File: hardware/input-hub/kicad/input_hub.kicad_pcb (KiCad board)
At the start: 2 copper layers, 116 x 49.1 mm, 38 parts, among them J1 ACJMIH, J2 ACJMIH, J3 ACJMIH, J5 8P8C, J6 BM04B-SRSS-TB_LF__SN_, J7 Conn_01x04, J8 Conn_01x02, P1 S2B-PH-SM4-TB_LF__SN_, U1 102010448, U2 TPD4E05U06DQAR, U3 TPD4E05U06DQAR

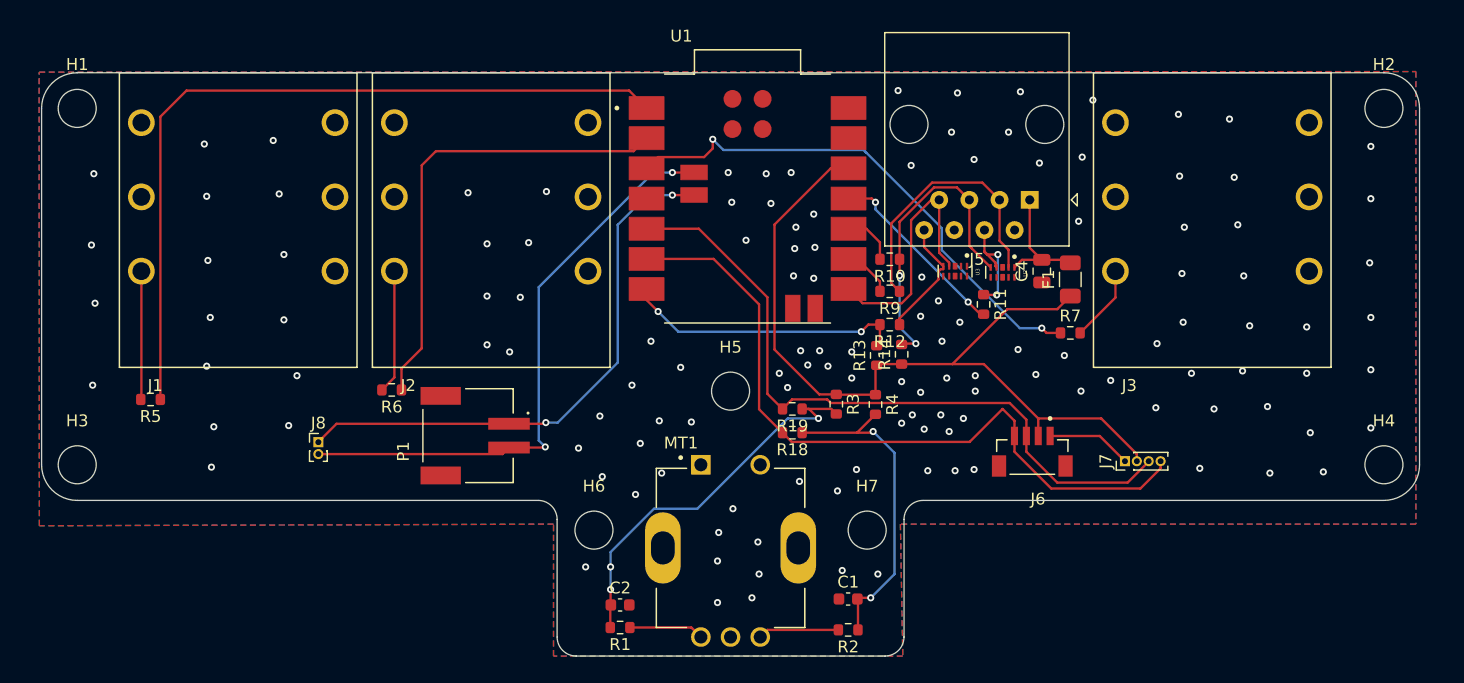
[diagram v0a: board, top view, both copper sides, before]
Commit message: fix: refine input hub board draft
Update the input hub KiCad design after
  layout review.

  - Replace solder fallback headers with standard 2.54 mm footprints.
  - Clean up PMW3610 RJ45 routing, ESD placement, and local power conditioning.
  - Add optional SJ1-3523N 3.5 mm jack library assets for future pedal jack variants.
  - Preserve AS5600, EC11, footswitch, battery, and PMW3610 interface options for review.
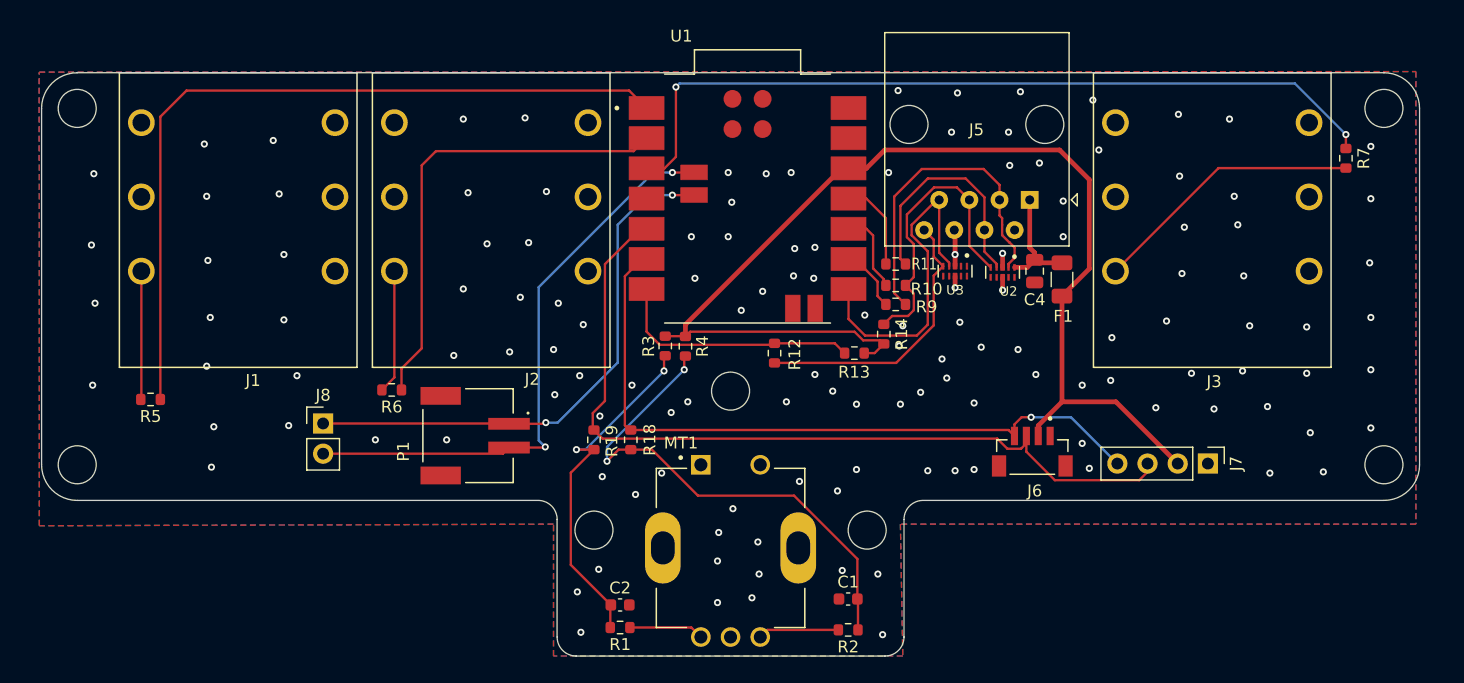
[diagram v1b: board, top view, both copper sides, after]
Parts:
- J7: footprint Connector_PinHeader_1.00mm:PinHeader_1x04_P1.00mm_Vertical -> Connector_PinHeader_2.54mm:PinHeader_1x04_P2.54mm_Vertical
- J8: footprint Connector_PinHeader_1.00mm:PinHeader_1x02_P1.00mm_Vertical -> Connector_PinHeader_2.54mm:PinHeader_1x02_P2.54mm_Vertical
- moved R7 27.5 mm to (206.8, 64.2), turned to -90 degrees
- moved R19 16.9 mm to (143.5, 87.9), turned to 90 degrees
- moved R4 16.7 mm to (151.2, 80.0)
- moved R3 15.2 mm to (149.5, 80.0)
- moved R18 13.6 mm to (146.6, 87.9), turned to 90 degrees
- moved R12 9.99 mm to (158.7, 80.6), turned to 90 degrees
- moved R11 8.14 mm to (168.9, 73.1), turned to 180 degrees
- moved J7 6.98 mm to (195.2, 89.9), turned to -90 degrees
- moved R14 2.27 mm to (167.9, 79.0)
- moved R10 2.26 mm to (168.9, 74.9)
- moved R13 1.89 mm to (165.4, 80.6), turned to 180 degrees
- moved J8 1.62 mm to (120.7, 86.5)
- moved R9 1.21 mm to (168.9, 76.5)
- moved F1 0.70 mm to (182.9, 74.4)
- moved C4 0.60 mm to (180.6, 73.7)
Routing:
- net +3V3: track 70.8 -> 98.3 mm
- net Button3: track 44.2 -> 68.2 mm
- net Net-(J3-PadT): track 6.43 -> 23.0 mm
- net Net-(C1-Pad2): track 27.6 -> 42.9 mm
- net NRST_RJ45: track 10.3 -> 23.7 mm
- net ENC_A: track 58.9 -> 70.5 mm
- net SDIO_RJ45: track 9.35 -> 20.1 mm, vias 2 -> 0
- net Net-(U1-D10/MOSI): track 15.8 -> 7.69 mm, vias 2 -> 0
- net MOT_RJ45: track 21.3 -> 28.2 mm
- net SCK_RJ45: track 23.1 -> 27.5 mm
- net Net-(C2-Pad1): track 33.3 -> 30.1 mm, vias 3 -> 2
- net Net-(U1-D6/TX): track 23.8 -> 21.1 mm, vias 2 -> 0
- net Net-(U1-D9/MISO): track 4.54 -> 6.88 mm
- net ENC_B: track 61.6 -> 59.8 mm, vias 0 -> 1
- net NCS_RJ45: track 26.3 -> 25.0 mm, vias 2 -> 0
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
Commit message: fix: refine input hub battery layout
- Update the battery connector layout.
  - Rename the battery connector from P to J.
  - Add return vias near signal vias.
  - Widen power-path traces.
  - Add XIAO battery solder holes and silkscreen labels.
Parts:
- added J10: Conn_01x01_Pin, Connector_Pin:Pin_D0.7mm_L6.5mm_W1.8mm_FlatFork, F.Cu at (151.9, 67.3)
- added J9: Conn_01x01_Pin, Connector_Pin:Pin_D0.7mm_L6.5mm_W1.8mm_FlatFork, F.Cu at (151.9, 65.4)
- moved J8 16.3 mm to (137.0, 86.3)
- moved J11 7.23 mm to (129.1, 87.5)
- moved R6 6.11 mm to (132.6, 83.1)
- renumbered P1 to J11
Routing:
- net BAT+: track 46.1 -> 36.4 mm, vias 2 -> 0
- net Button2: track 39.5 -> 30.2 mm
- net BAT-: track 49.8 -> 45.8 mm, vias 2 -> 0
- net Net-(J2-PadT): track 10.4 -> 11.5 mm
- net ENC_A: track 70.5 -> 69.7 mm
- net GND: vias 136 -> 143
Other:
- board text added: "BAT+"
- board text added: "BAT-"

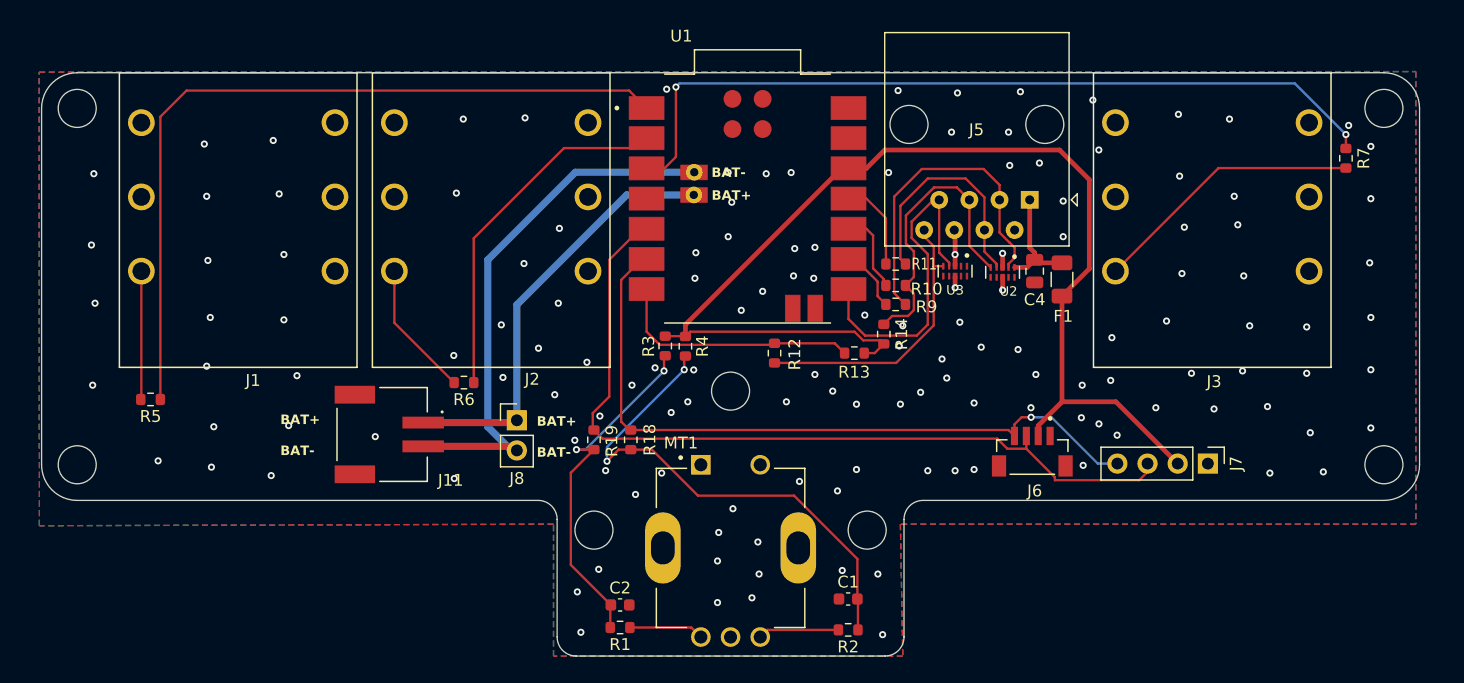
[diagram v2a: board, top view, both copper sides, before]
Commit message: fix: make input hub routing more gooder and a schematic change - esd routing and schematic - PEC11R debounce circuit - reduced back side routing - added filter caps to 1/4 inch jacks - made traces thiccer
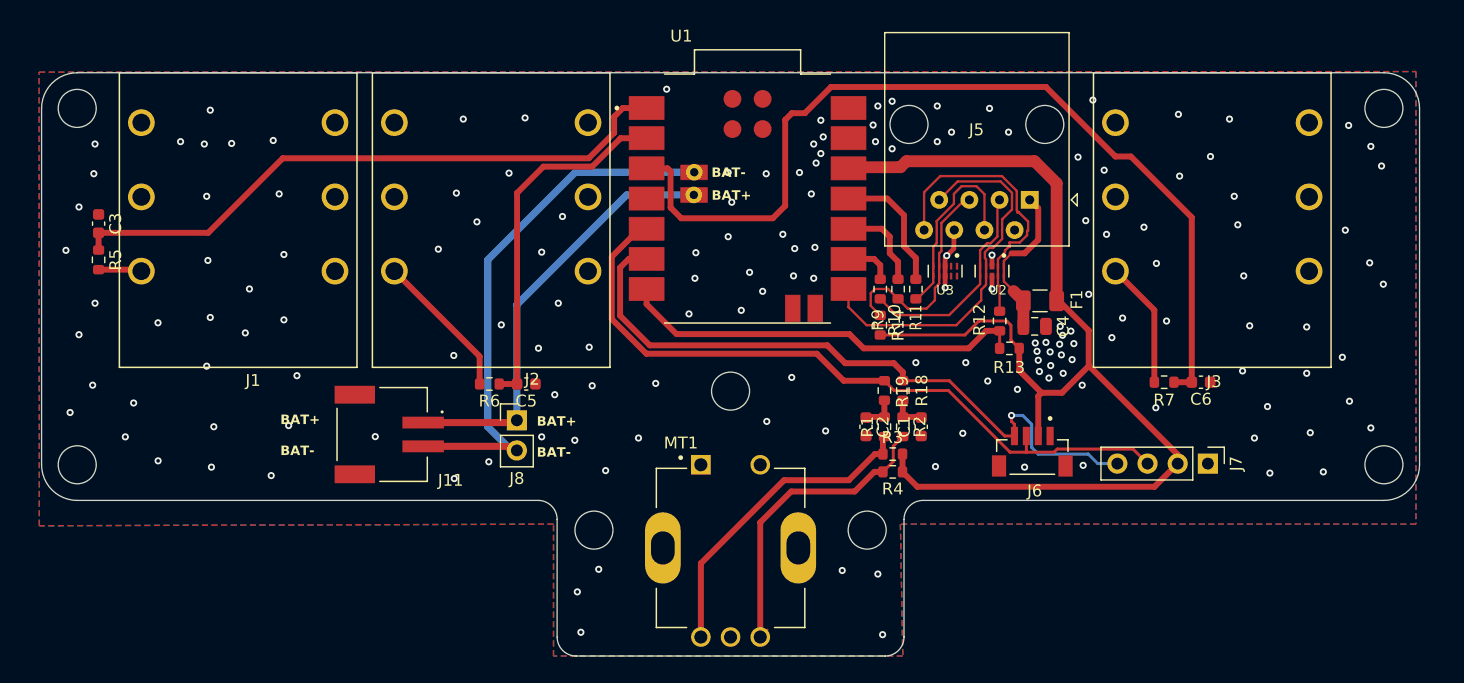
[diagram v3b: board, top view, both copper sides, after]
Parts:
- added C3: 1u, Capacitor_SMD:C_0603_1608Metric, F.Cu at (101.8, 69.7)
- added C5: 1u, Capacitor_SMD:C_0603_1608Metric, F.Cu at (137.8, 83.2)
- added C6: 1u, Capacitor_SMD:C_0603_1608Metric, F.Cu at (194.6, 83.0)
- moved R1 27.9 mm to (167.9, 86.8), turned to 90 degrees
- moved C2 25.6 mm to (166.4, 86.8), turned to -90 degrees
- moved R19 24.8 mm to (167.9, 83.8)
- moved R7 24.3 mm to (191.5, 83.0), turned to 180 degrees
- moved R18 23.3 mm to (169.5, 83.8)
- moved R3 21.2 mm to (168.7, 89.1), turned to 180 degrees
- moved R4 20.4 mm to (168.7, 90.6), turned to 180 degrees
- moved R12 19.1 mm to (177.7, 77.9), turned to -90 degrees
- moved R2 17.7 mm to (169.5, 86.8), turned to -90 degrees
- moved C1 15.8 mm to (171.1, 86.8), turned to 90 degrees
- moved R13 13.1 mm to (178.5, 80.2)
- moved R5 12.5 mm to (101.8, 72.8), turned to -90 degrees
- moved C4 4.65 mm to (180.6, 78.3), turned to 180 degrees
- moved R11 2.71 mm to (170.6, 75.2), turned to 90 degrees
- moved F1 2.58 mm to (181.1, 76.2), turned to 180 degrees
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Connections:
- R3 pad 2: Net-(C2-Pad1) -> Net-(MT1-PadA)
- R4 pad 2: Net-(C1-Pad2) -> Net-(MT1-PadB)
- U2 pad 10: unconnected-(U2-NC_10-Pad10) -> 3V3_RJ45
- U2 pad 2: SCK_RJ45 -> NRST_RJ45
- U2 pad 4: SDIO_RJ45 -> MOT_RJ45
- U2 pad 5: NCS_RJ45 -> SCK_RJ45
- U2 pad 6: unconnected-(U2-NC_6-Pad6) -> SCK_RJ45
- U2 pad 7: unconnected-(U2-NC_7-Pad7) -> MOT_RJ45
- U2 pad 9: unconnected-(U2-NC_9-Pad9) -> NRST_RJ45
- U3 pad 4: MOT_RJ45 -> NCS_RJ45
- U3 pad 5: NRST_RJ45 -> SDIO_RJ45
- U3 pad 6: unconnected-(U3-NC_6-Pad6) -> SDIO_RJ45
- U3 pad 7: unconnected-(U3-NC_7-Pad7) -> NCS_RJ45
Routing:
- net Net-(C1-Pad2): track 42.9 -> 2.97 mm, vias 2 -> 0
- net Net-(C2-Pad1): track 30.1 -> 2.97 mm, vias 2 -> 0
- net Net-(MT1-PadA): track 6.31 -> 26.9 mm
- net Net-(MT1-PadB): track 6.82 -> 26.3 mm
- net Button1: track 66.3 -> 52.7 mm
- net Net-(U1-D6/TX): track 21.1 -> 34.6 mm
- net Net-(J3-PadT): track 23.0 -> 10.7 mm
- net Button3: track 68.2 -> 78.2 mm, vias 2 -> 0
- net SCK_RJ45: track 27.5 -> 18.0 mm
- net ENC_A: track 69.7 -> 61.6 mm
- net Net-(J1-PadT): track 10.8 -> 3.65 mm
- net NCS_RJ45: track 25.0 -> 18.6 mm
- net 3V3_RJ45: track 9.59 -> 13.6 mm
- net SDIO_RJ45: track 20.1 -> 16.4 mm
- net MOT_RJ45: track 28.4 -> 31.8 mm
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
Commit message: feat: add PJ-307 alternate pedal jacks
- Import the HOOYA PJ-307/C2939173 symbol, footprint, and STEP model.
  - Replace the stale SJ1-3523N library assets with the PJ-307 part.
  - Add 3.5 mm alternate pedal jack footprints under the 1/4 in pedal jacks.
  - Update silkscreen labels and artwork
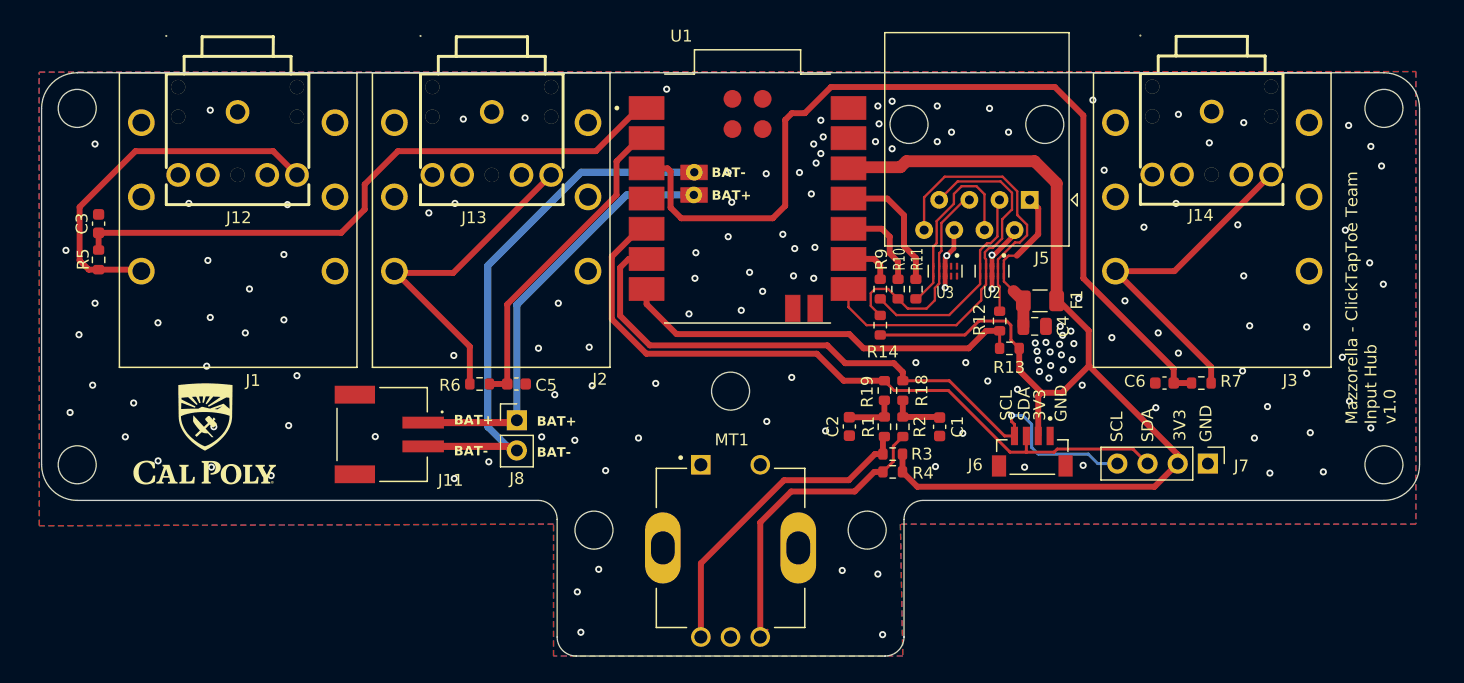
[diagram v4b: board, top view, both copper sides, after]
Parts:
- added J12: PJ-307, input_hub:AUDIO-TH_PJ-307, F.Cu at (113.5, 63.0)
- added J13: PJ-307, input_hub:AUDIO-TH_PJ-307, F.Cu at (134.9, 63.0)
- added J14: PJ-307, input_hub:AUDIO-TH_PJ-307, F.Cu at (195.5, 62.9)
- moved R7 3.13 mm to (194.6, 83.1), turned to 0 degrees
- moved C6 3.07 mm to (191.5, 83.1), turned to 0 degrees
- moved C1 1.55 mm to (172.6, 86.8)
- moved C2 1.40 mm to (165.0, 86.8)
- moved C5 0.83 mm to (137.0, 83.2)
- moved R6 0.82 mm to (133.9, 83.2)
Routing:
- net Net-(J1-PadT): track 3.65 -> 31.1 mm
- net Net-(J14-Pad2): track 10.7 -> 29.2 mm
- net Net-(J13-Pad2): track 12.5 -> 28.8 mm
- net GND: track 7.43 -> 11.3 mm, vias 162 -> 147
- net Button2: track 30.4 -> 27.4 mm
- net Net-(C1-Pad2): track 2.97 -> 4.52 mm
- net Net-(C2-Pad1): track 2.97 -> 4.36 mm
- net Button3: track 78.2 -> 77.3 mm
- net NRST_RJ45: track 24.4 -> 23.6 mm
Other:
- board text added: "3V3"
- board text added: "GND"
- board text added: "Mazzorella - ClickTapToe Team Input Hub v1.0"
- board text added: "SCL"
- board text added: "SDA"

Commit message: feat: remove input hub EC11 encoder and update 3D models
- Remove the EC11 encoder and supporting debounce network from the input hub.
  - Add project-local 3D model links for imported input hub footprints.
  - Vendor the RJ45 footprint with the exact Amphenol 54602-908LF model.
  - Add the XIAO battery solder access symbol and footprint.
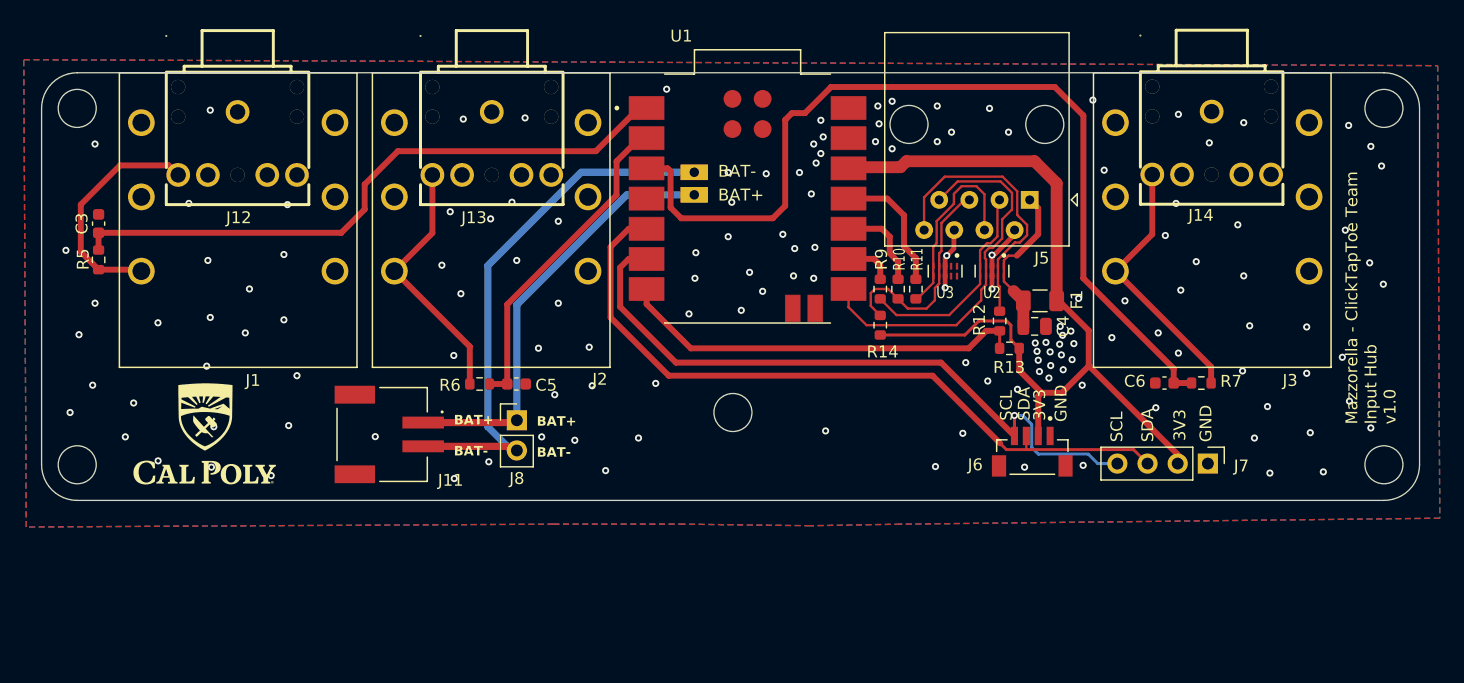
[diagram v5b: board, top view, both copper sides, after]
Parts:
- removed C1, C2: 10nF, Capacitor_SMD:C_0603_1608Metric
- removed H6, H7: MountingHole, MountingHole:MountingHole_3.2mm_M3_ISO14580
- removed J9: Conn_01x01_Pin, Connector_Pin:Pin_D0.7mm_L6.5mm_W1.8mm_FlatFork
- removed MT1: PEC11R-4215F-S0024, input_hub:XDCR_PEC11R-4215F-S0024
- removed R1, R2, R3, R4: 10k, Resistor_SMD:R_0603_1608Metric
- removed R18, R19: 0R, Resistor_SMD:R_0603_1608Metric
- J10: value Conn_01x01_Pin -> XIAO_BAT_SOLDER_ACCESS; footprint Connector_Pin:Pin_D0.7mm_L6.5mm_W1.8mm_FlatFork -> input_hub:XIAO_BAT_SOLDER_ACCESS
- J5: value 8P8C -> 54602-908LF; footprint Connector_RJ:RJ45_Amphenol_54602-x08_Horizontal -> input_hub:RJ45_Amphenol_54602-x08_Horizontal
- moved J10 1.91 mm to (151.9, 65.4)
- moved H5 1.81 mm to (155.2, 85.6)
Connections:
- J12 pad 2: Net-(J1-PadT) -> unconnected-(J12-Pad2)
- J12 pad 5: unconnected-(J12-Pad5) -> Net-(J1-PadT)
- J13 pad 2: Net-(J13-Pad2) -> unconnected-(J13-Pad2)
- J13 pad 5: unconnected-(J13-Pad5) -> Net-(J13-Pad5)
- J14 pad 2: Net-(J14-Pad2) -> unconnected-(J14-Pad2)
- J14 pad 5: unconnected-(J14-Pad5) -> Net-(J14-Pad5)
- J2 pad T: Net-(J13-Pad2) -> Net-(J13-Pad5)
- J3 pad T: Net-(J14-Pad2) -> Net-(J14-Pad5)
- R6 pad 2: Net-(J13-Pad2) -> Net-(J13-Pad5)
- R7 pad 2: Net-(J14-Pad2) -> Net-(J14-Pad5)
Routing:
- net Net-(J14-Pad2): track 29.2 -> 0.00 mm
- net Net-(J13-Pad2): track 28.8 -> 0.00 mm
- net Net-(MT1-PadA): track 26.9 -> 0.00 mm
- net Net-(MT1-PadB): track 26.3 -> 0.00 mm
- net +3V3: track 100.1 -> 74.1 mm
- net Net-(J14-Pad5): track 0.00 -> 22.2 mm
- net Net-(J13-Pad5): track 0.00 -> 21.6 mm
- net Net-(J1-PadT): track 31.1 -> 19.6 mm
- net Net-(C1-Pad2): track 4.52 -> 0.00 mm
- net Net-(C2-Pad1): track 4.36 -> 0.00 mm
- net ENC_B: track 58.0 -> 56.7 mm
- net GND: vias 147 -> 145
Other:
- board size 116 x 49.1 mm -> 116 x 36 mm
